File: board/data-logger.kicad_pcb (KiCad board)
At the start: 6 copper layers, 58 x 88 mm, 253 parts, among them IC201 ATTINY2313-MU, P201 CONN_01X02, P301 CONN_02X11, P302 CONN_02X11, P303 CONN_02X11, P601 CONN_02X06, P602 CONN_02X06, P701 USB_B_3, Q203 CSD17313Q2, Q204 CSD17313Q2, Q205 FDG1024NZ, U202 CYUSB3012-BZXC, U204 NCP373MU13TXG, U208 MIC23050-4YML, U210 TLV62085, U211 TPS53015, U212 TLV62085, U213 NCP380, U214 NCP380, U215 TLV62085, U301 5CEFA2F23, U302 TS881ICT, U303 FSA5157P6X, U304 FSA5157P6X, U305 TS881ICT, U306 FSA5157P6X, U307 TS881ICT, U401 IS43TR16256LA, U402 DSC1103CI5-100.0000, U403 NCP51200, U501 25LC_EEPROM, U503 SI5351A-B-GT, U701 NCP361SNT1G, U702 SP3010-04UTG, X701 CONN_DEBUG_MCNET, X702 ASDMB-19.200MHZ-LC-T, Y501 25.000MHz

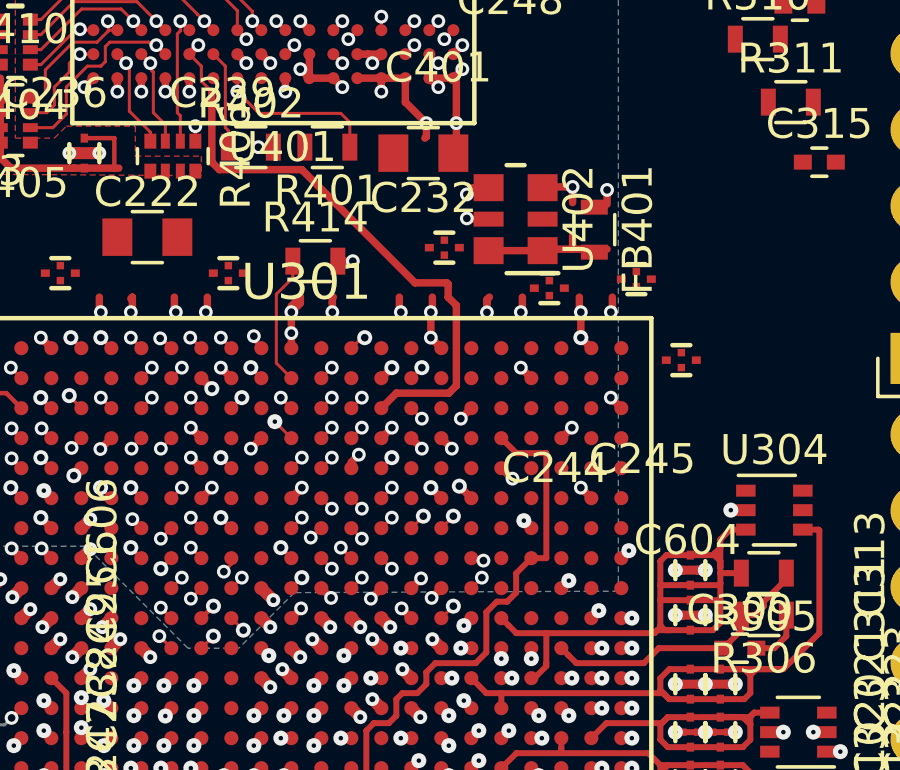
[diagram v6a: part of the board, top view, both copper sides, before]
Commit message: Fix input clock assignment for PLLs
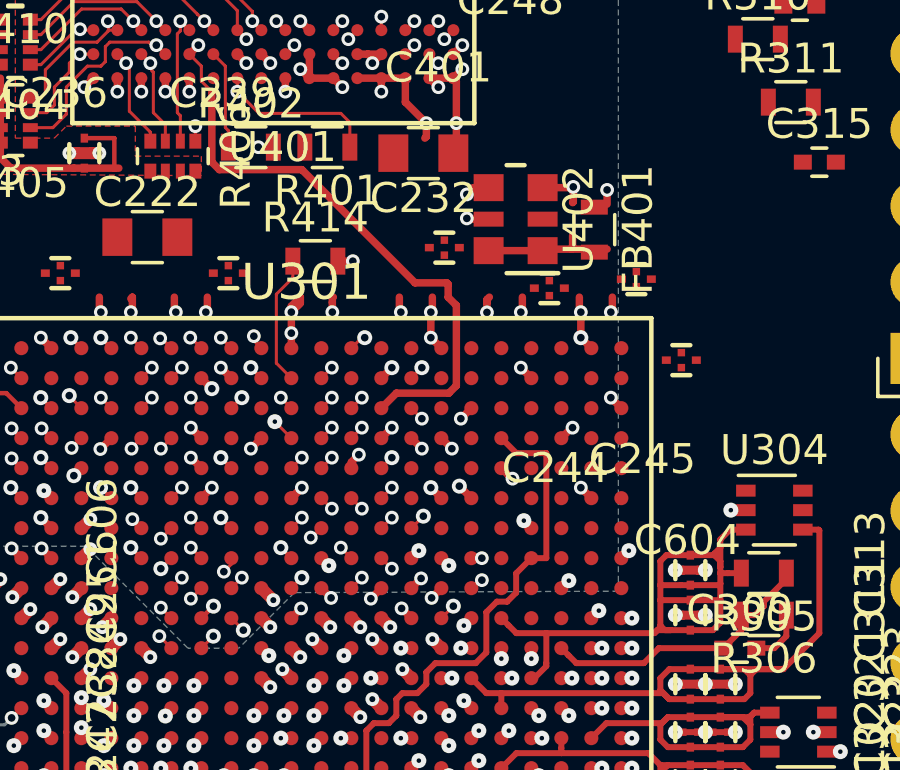
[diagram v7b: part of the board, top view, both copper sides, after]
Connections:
- U301 pad AA22: (no net) -> /Cyclone V User IO/IO_A7_P
- U301 pad AB22: (no net) -> /Cyclone V User IO/IO_A7_N
- U301 pad G13: /Cyclone V DDR3 RAM/FPGA_CLK10_N -> (no net)
- U301 pad H13: /Cyclone V DDR3 RAM/FPGA_CLK10_P -> FPGA_CLK1
- U301 pad H15: (no net) -> /Cyclone V DDR3 RAM/FPGA_CLK10_N
- U301 pad H16: (no net) -> /Cyclone V DDR3 RAM/FPGA_CLK10_P
- U301 pad M9: /Cyclone V FX3 FIFO/FPGA_CLK0 -> (no net)
- U301 pad N9: /Cyclone V FX3 FIFO/FPGA_CLK1 -> /Cyclone V FX3 FIFO/FPGA_CLK0
- U301 pad P9: /Cyclone V FX3 FIFO/FPGA_CLK2 -> (no net)
- U301 pad V16: /Cyclone V User IO/IO_A7_N -> (no net)
- U301 pad W16: /Cyclone V User IO/IO_A7_P -> FPGA_CLK2
- U503 pad 6: /Cyclone V FX3 FIFO/FPGA_CLK2 -> FPGA_CLK2
- U503 pad 9: /Cyclone V FX3 FIFO/FPGA_CLK1 -> FPGA_CLK1
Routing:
- net /Cyclone V DDR3 RAM/FPGA_CLK10_P: track 20.7 -> 16.5 mm
- net /Cyclone V DDR3 RAM/FPGA_CLK10_N: track 20.6 -> 18.6 mm
- net (no net): track 13.5 -> 13.0 mm, vias 14 -> 13
- net FPGA_CLK1: track 0.00 -> 0.49 mm, vias 0 -> 1

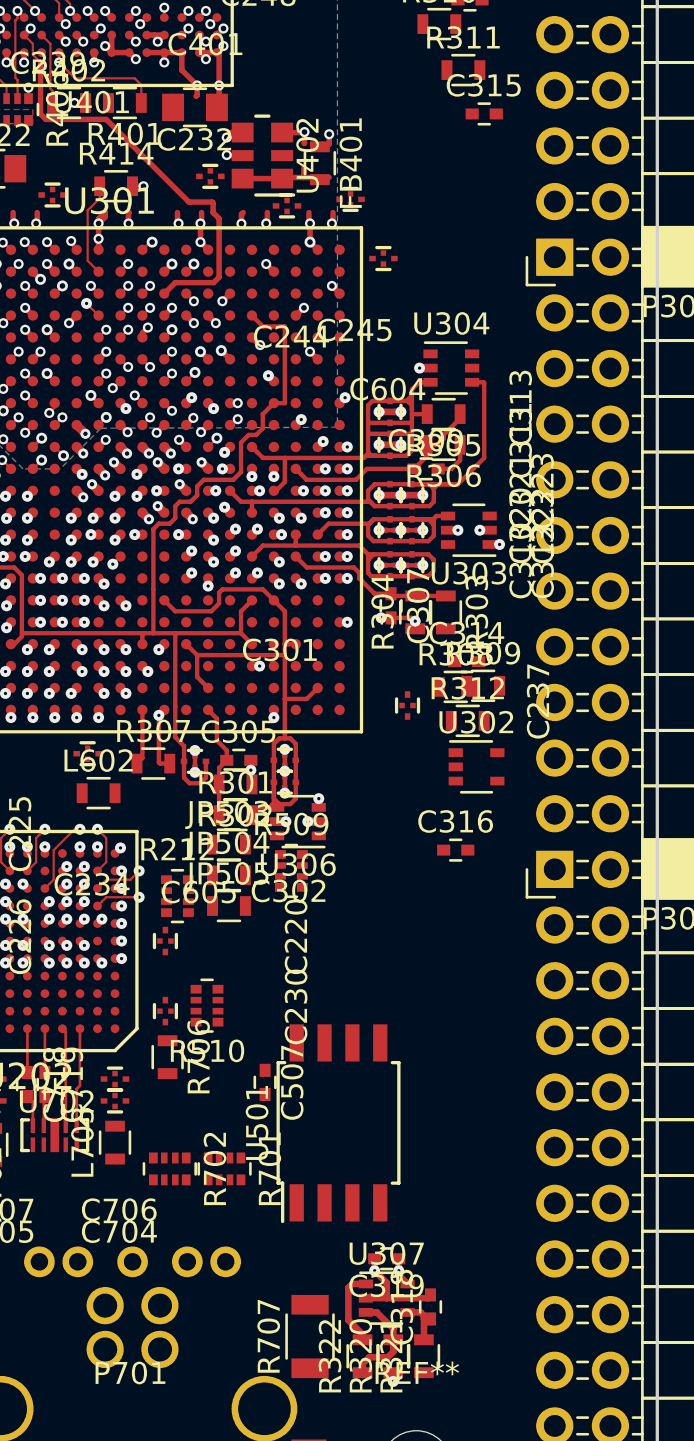
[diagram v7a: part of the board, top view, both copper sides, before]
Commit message: General circuit work
- Change io power switch iv
- reassign some user io pins to improve layout
- escape route user io lines from fpga
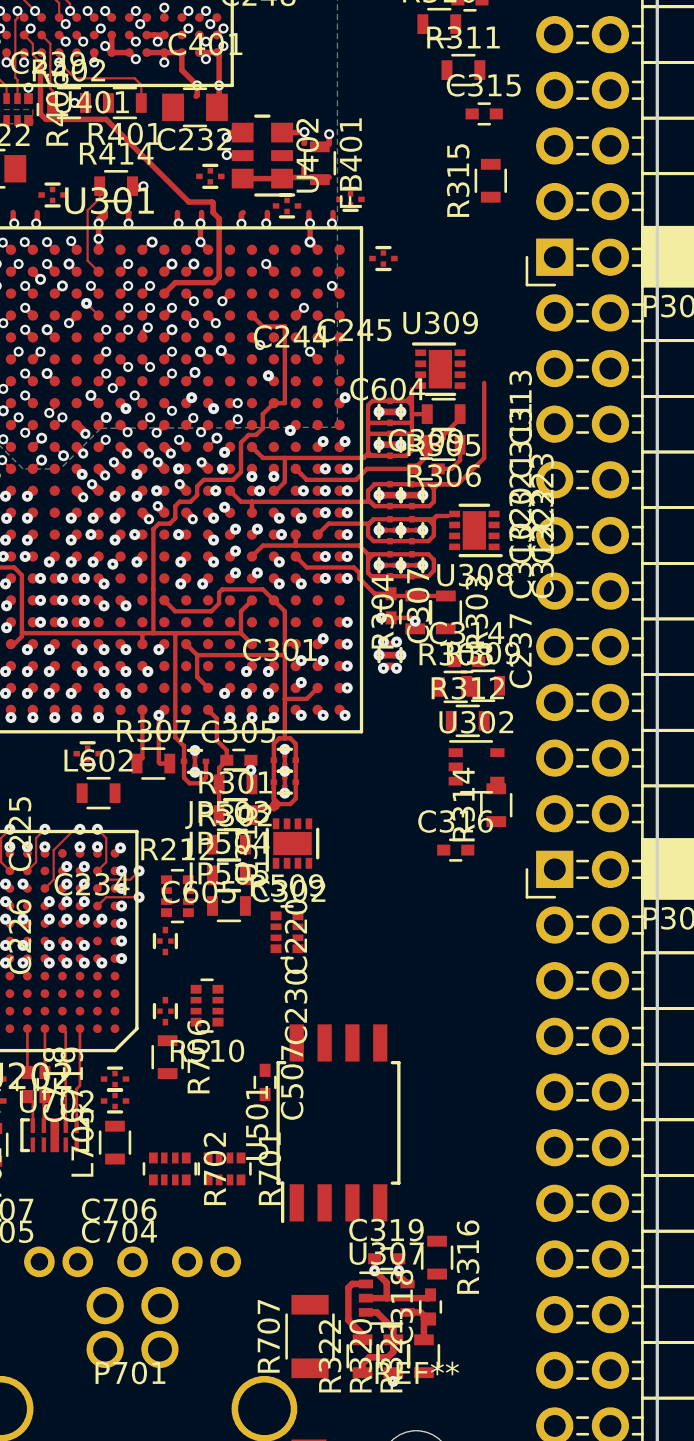
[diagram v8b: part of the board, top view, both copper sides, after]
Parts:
- removed U303, U304, U306: FSA5157P6X, TO_SOT_Packages_SMD:SOT-363_SC-70-6
- added R314: 100k, Resistors_SMD:R_0603, F.Cu at (129.2, 128.3)
- added R315: 100k, Resistors_SMD:R_0603, F.Cu at (128.9, 99.8)
- added R316: 100k, Resistors_SMD:R_0603, F.Cu at (126.5, 149.0)
- added U308: SiP32413, Housings_DFN_QFN:DFN-8-1EP_2x2mm_Pitch0.5mm, F.Cu at (128.2, 115.8)
- added U309: SiP32413, Housings_DFN_QFN:DFN-8-1EP_2x2mm_Pitch0.5mm, F.Cu at (126.6, 108.5)
- added U310: SiP32413, Housings_DFN_QFN:DFN-8-1EP_2x2mm_Pitch0.5mm, F.Cu at (119.8, 130.1)
- moved R509 2.81 mm to (119.6, 134.2)
- moved C237 2.44 mm to (124.3, 121.5)
- turned C319 to 0 degrees
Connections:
- C316 pad 1: VCC_3V30_FPGA -> GND
- C316 pad 2: GND -> VCC_3V30_FPGA
- C317 pad 1: VCC_3V30_FPGA -> GND
- C317 pad 2: GND -> VCC_3V30_FPGA
- C319 pad 1: /Cyclone V User IO/VCC_3V30 -> GND
- C319 pad 2: GND -> VCC_3V30_FPGA
- R312 pad 1: Net-(R308-Pad2) -> Net-(R312-Pad1)
- R312 pad 2: Net-(R312-Pad2) -> Net-(R308-Pad2)
- R322 pad 1: Net-(R320-Pad2) -> Net-(R322-Pad1)
- R322 pad 2: Net-(R322-Pad2) -> Net-(R320-Pad2)
- U301 pad AA13: /Cyclone V User IO/IO_A2_P -> (no net)
- U301 pad AA14: /Cyclone V User IO/IO_A2_N -> (no net)
- U301 pad AA15: /Cyclone V User IO/IO_A3_P -> (no net)
- U301 pad AA17: (no net) -> /Cyclone V User IO/IO_A3_N
- U301 pad AA18: (no net) -> /Cyclone V User IO/IO_A3_P
- U301 pad AA19: (no net) -> /Cyclone V User IO/IO_A5_N
- U301 pad AA20: (no net) -> /Cyclone V User IO/IO_A5_P
- U301 pad AB15: /Cyclone V User IO/IO_A3_N -> (no net)
- U301 pad AB20: (no net) -> /Cyclone V User IO/IO_A1_N
- U301 pad AB21: (no net) -> /Cyclone V User IO/IO_A1_P
- U301 pad H13: FPGA_CLK1 -> (no net)
- U301 pad K17: /Cyclone V User IO/IO_C4_P -> /Cyclone V User IO/IO_C1_P
- U301 pad L17: /Cyclone V User IO/IO_C4_N -> /Cyclone V User IO/IO_C1_N
- U301 pad L18: /Cyclone V User IO/IO_C6_N -> /Cyclone V User IO/IO_C3_N
- U301 pad L19: /Cyclone V User IO/IO_C6_P -> /Cyclone V User IO/IO_C3_P
- U301 pad L22: /Cyclone V User IO/IO_C3_N -> /Cyclone V User IO/IO_C5_N
- U301 pad M20: /Cyclone V User IO/IO_C5_P -> /Cyclone V User IO/IO_C6_P
- U301 pad M21: /Cyclone V User IO/IO_C5_N -> /Cyclone V User IO/IO_C6_N
- U301 pad M22: /Cyclone V User IO/IO_C3_P -> /Cyclone V User IO/IO_C5_P
- U301 pad M9: (no net) -> /Cyclone V FX3 FIFO/FPGA_CLK1
- U301 pad N20: /Cyclone V User IO/IO_C1_P -> /Cyclone V User IO/IO_C4_P
- U301 pad N21: /Cyclone V User IO/IO_C1_N -> /Cyclone V User IO/IO_C4_N
- U301 pad T12: /Cyclone V User IO/IO_A1_N -> (no net)
- U301 pad T13: /Cyclone V User IO/IO_A1_P -> (no net)
- U301 pad U13: /Cyclone V User IO/IO_A0_P -> (no net)
- U301 pad V13: /Cyclone V User IO/IO_A0_N -> (no net)
- U301 pad V14: /Cyclone V User IO/IO_A5_N -> (no net)
- U301 pad V15: /Cyclone V User IO/IO_A5_P -> (no net)
- U301 pad W21: (no net) -> /Cyclone V User IO/IO_A2_P
- U301 pad W22: (no net) -> /Cyclone V User IO/IO_A0_P
- U301 pad Y14: /Cyclone V User IO/IO_A4_N -> (no net)
- U301 pad Y15: /Cyclone V User IO/IO_A4_P -> (no net)
- U301 pad Y19: (no net) -> /Cyclone V User IO/IO_A4_P
- U301 pad Y20: (no net) -> /Cyclone V User IO/IO_A4_N
- U301 pad Y21: (no net) -> /Cyclone V User IO/IO_A2_N
- U301 pad Y22: (no net) -> /Cyclone V User IO/IO_A0_N
- U302 pad 1: Net-(R312-Pad2) -> Net-(R312-Pad1)
- U307 pad 1: Net-(R322-Pad2) -> Net-(R322-Pad1)
- U307 pad 5: /Cyclone V User IO/VCC_3V30 -> VCC_3V30_FPGA
- U503 pad 9: FPGA_CLK1 -> /Cyclone V FX3 FIFO/FPGA_CLK1
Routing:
- net /Cyclone V User IO/IO_C3_N: track 31.7 -> 10.6 mm
- net /Cyclone V User IO/IO_C3_P: track 29.0 -> 9.72 mm
- net /Cyclone V User IO/IO_C1_N: track 27.8 -> 11.4 mm
- net /Cyclone V User IO/IO_C1_P: track 25.6 -> 11.2 mm
- net /Cyclone V User IO/IO_C4_P: track 29.0 -> 39.6 mm
- net /Cyclone V User IO/IO_C0_N: track 24.8 -> 34.3 mm
- net /Cyclone V User IO/IO_C0_P: track 22.8 -> 32.2 mm
- net /Cyclone V User IO/IO_B3_N: track 12.5 -> 21.6 mm
- net /Cyclone V User IO/IO_B3_P: track 9.03 -> 17.9 mm
- net /Cyclone V User IO/IO_B7_N: track 15.6 -> 7.58 mm
- net /Cyclone V User IO/IO_C4_N: track 32.3 -> 40.0 mm
- net /Cyclone V User IO/IO_B1_N: track 11.7 -> 18.6 mm
- net /Cyclone V User IO/IO_B5_P: track 9.33 -> 15.8 mm
- net /Cyclone V User IO/IO_A2_P: track 24.3 -> 30.5 mm, vias 0 -> 1
- net /Cyclone V User IO/IO_B1_P: track 9.03 -> 14.8 mm
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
